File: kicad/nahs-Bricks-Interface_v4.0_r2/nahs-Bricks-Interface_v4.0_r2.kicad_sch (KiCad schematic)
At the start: 43 parts, among them J1 Brick-Interface-V4, J2 Brick-Interface-V4, J3 TE_292304-1, J4 TE_292303-1, SW1 K3-2336S-F1, SW2 K3-2336S-F1, SW3 K3-2336S-F1, SW4 Taster_4545, U1 SL2.1A, U2 CP2102N-A02-GQFN20R, Y1 12MHz

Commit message: v4.0 r2 ibom done
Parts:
- C10, C3, C4, C5, C6, C8, C9: Storage (none) -> MAG4
- C11, C7: Storage (none) -> SK1 4x1; StorageDesc (none) -> 100µF
- D1: Desc PWD -> PWR; Storage (none) -> MAG4; StorageDesc (none) -> LED OrangeRed
- D2: Storage (none) -> MAG4; StorageDesc (none) -> LED OrangeRed
- D3, D4: Storage (none) -> MAG4; StorageDesc (none) -> LED Green
- F1: Storage (none) -> SK1 4x4; StorageDesc (none) -> Fuse 50mA
- FID1, FID2, FID3, JP1, JP2, JP3, JP4, JP5, JP6, LOGO1, LOGO2: DNP (none) -> true
- J1: Handsolder (none) -> true; Storage (none) -> SK2 1x4; StorageDesc (none) -> PCIE 1x THD
- J2: Handsolder (none) -> true; Storage (none) -> SK2 1x4; StorageDesc (none) -> PCIE 1x Straddle
- J3: Handsolder (none) -> true; Storage (none) -> SK2 1x3; StorageDesc (none) -> USB TypeB
- J4: Handsolder (none) -> true; Storage (none) -> SK2 1x3; StorageDesc (none) -> USB TypeA
- R1: Desc (none) -> MAG1; Storage (none) -> MAG1
- R2, R3: Storage (none) -> MAG2
- R4, R5, R6, R7: Storage (none) -> MAG1; StorageDesc (none) -> 6030
- SW1, SW2, SW3: Storage (none) -> SK1 2x2; StorageDesc (none) -> K3-2336S-F1
- SW4: Handsolder (none) -> true; Storage (none) -> SK1 4x3; StorageDesc (none) -> Taster 4545
- U1: Storage (none) -> SK1 4x4; StorageDesc (none) -> SL2.1A
- U2: Storage (none) -> SK1 4x4; StorageDesc (none) -> CP2102N-A02
- Y1: Storage (none) -> SK1 1x3; StorageDesc (none) -> Crystal 12MHz

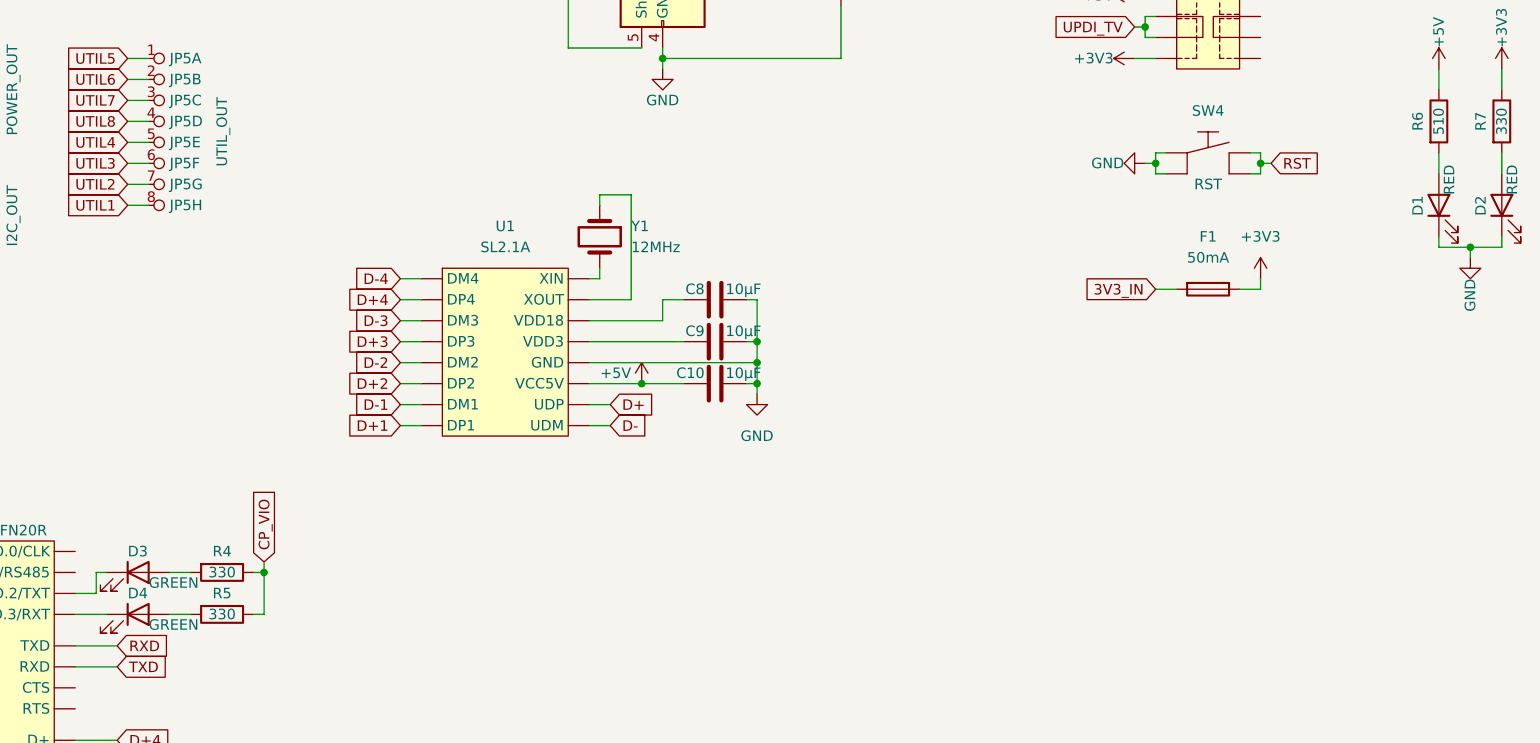
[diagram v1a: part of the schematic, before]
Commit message: changed colors of LEDs
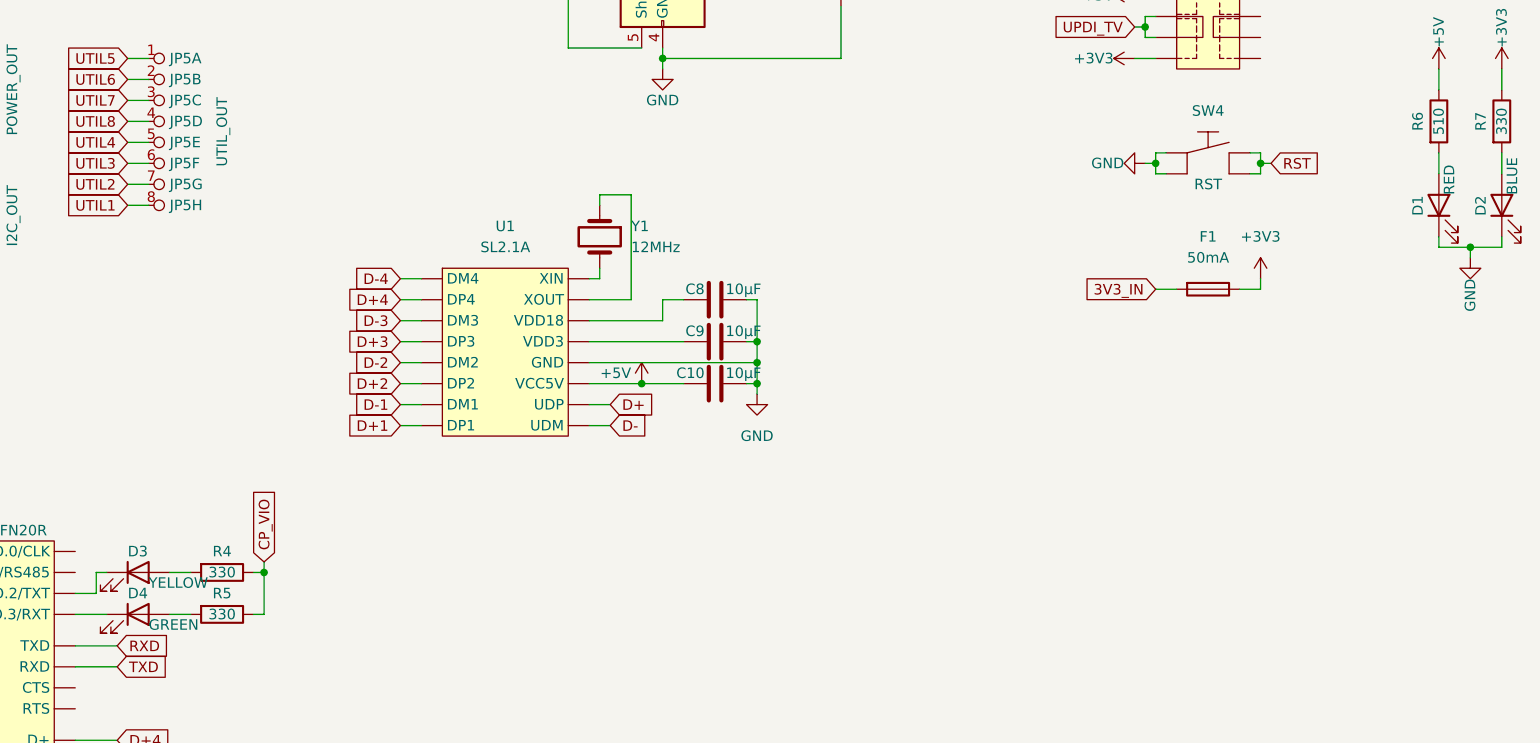
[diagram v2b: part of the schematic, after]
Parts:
- D2: value RED -> BLUE; StorageDesc LED OrangeRed -> LED Blue
- D3: value GREEN -> YELLOW; StorageDesc LED Green -> LED Yellow
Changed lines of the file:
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@@
       (effects (font (size 1.27 1.27)) (justify left))
     )
-    (property "Value" "RED" (id 1) (at 248.92 93.98 0)
+    (property "Value" "BLUE" (id 1) (at 248.92 93.98 0)
       (effects (font (size 1.27 1.27)) (justify left))
     )
@@
       (effects (font (size 1.27 1.27)) hide)
     )
-    (property "StorageDesc" "LED OrangeRed" (id 6) (at 247.65 95.25 0)
+    (property "StorageDesc" "LED Blue" (id 6) (at 247.65 95.25 0)
       (effects (font (size 1.27 1.27)) hide)
     )
@@
       (effects (font (size 1.27 1.27)) (justify left))
     )
-    (property "Value" "GREEN" (id 1) (at 83.82 140.97 0)
+    (property "Value" "YELLOW" (id 1) (at 83.82 140.97 0)
       (effects (font (size 1.27 1.27)) (justify left))
     )
@@
       (effects (font (size 1.27 1.27)) hide)
     )
-    (property "StorageDesc" "LED Green" (id 6) (at 82.55 139.7 0)
+    (property "StorageDesc" "LED Yellow" (id 6) (at 82.55 139.7 0)
       (effects (font (size 1.27 1.27)) hide)
     )
@@
     )
     (path "/7da976fa-6f84-4146-948f-0e2f7aad5359"
-      (reference "D2") (unit 1) (value "RED") (footprint "no_common:LED_0805_2012Metric")
+      (reference "D2") (unit 1) (value "BLUE") (footprint "no_common:LED_0805_2012Metric")
     )
     (path "/9aebf78f-d089-46be-ab22-640c2018930e"
-      (reference "D3") (unit 1) (value "GREEN") (footprint "no_common:LED_0805_2012Metric")
+      (reference "D3") (unit 1) (value "YELLOW") (footprint "no_common:LED_0805_2012Metric")
     )
     (path "/73bf4caf-66fe-4bf7-8394-780453d5048a"
